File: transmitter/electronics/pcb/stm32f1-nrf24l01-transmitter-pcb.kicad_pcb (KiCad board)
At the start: 2 copper layers, 128 x 47 mm, 79 parts, among them J1 PA1/A1, J10 PB3, J11 PB4, J12 PB5, J13 PB6, J14 PB7, J15 PB8, J16 PB10, J17 PB11, J18 External charger LED, J19 BATTERY, J2 PA2/A2, J20 Red, J21 Blue, J22 POWER SWITCH, J23 USB, J24 UART, J25 SWD, J26 Buzzer, J27 NRF24 connector, J29 Meter, J3 PA3/A3, J30 LED, J4 PA4/A4, J5 PA5/A5, J6 PA6/A6, J7 PA7/A7, J8 PB0/A8, J9 PB1/A9, Q1 PMV30UN, SW1 RESET, U1 MCP1703A-3302, U2 LIPO_CHARGER_+_PROTECTION, U3 STM32F103CBT6, U4 MCP1703A-3302, Y1 8MHz

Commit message: Tweak layout
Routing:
- net /+USB: track 25.9 -> 37.4 mm
- net +3V3: track 294.7 -> 302.2 mm
- net /PB4: track 26.1 -> 24.3 mm
- net /PB3: track 31.9 -> 30.3 mm
- net /PB7: track 16.1 -> 14.6 mm
- net Net-(J18-Pad2): track 7.47 -> 6.13 mm
- net Net-(J22-Pad1): track 25.0 -> 24.1 mm
- net Net-(J18-Pad1): track 6.11 -> 5.37 mm

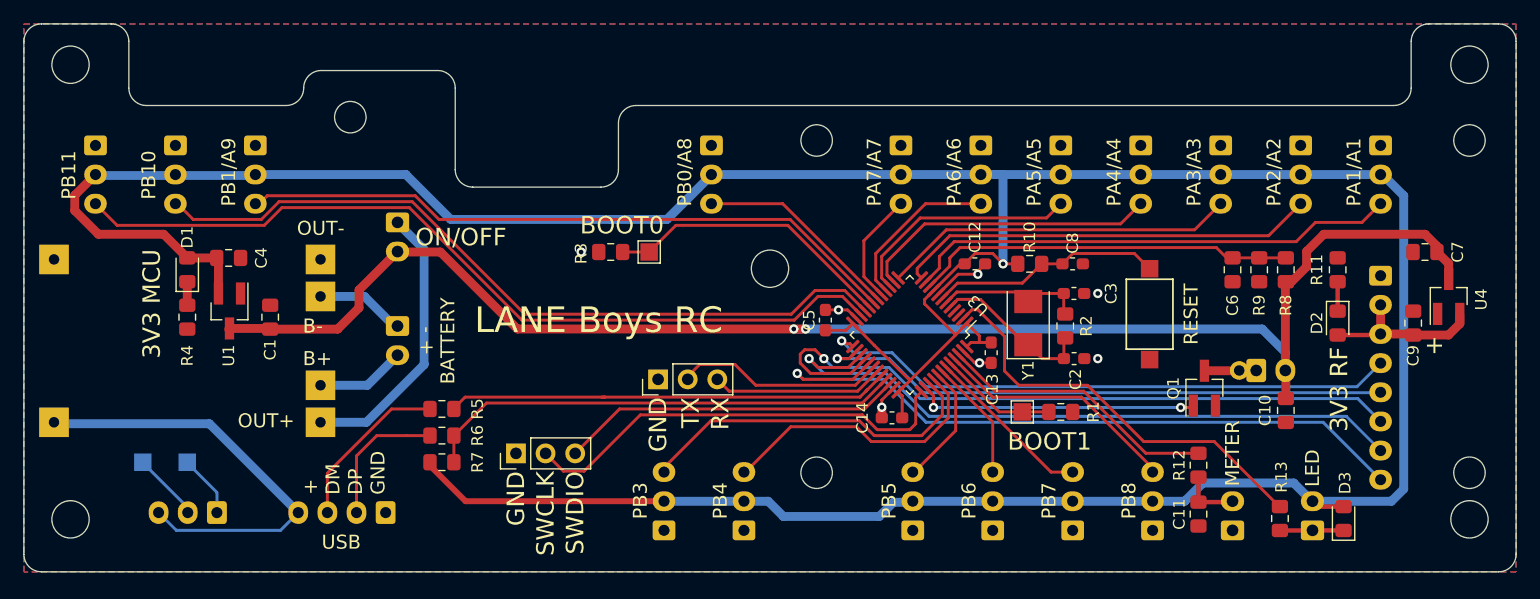
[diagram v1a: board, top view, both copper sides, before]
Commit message: Improve placement and silkscreen
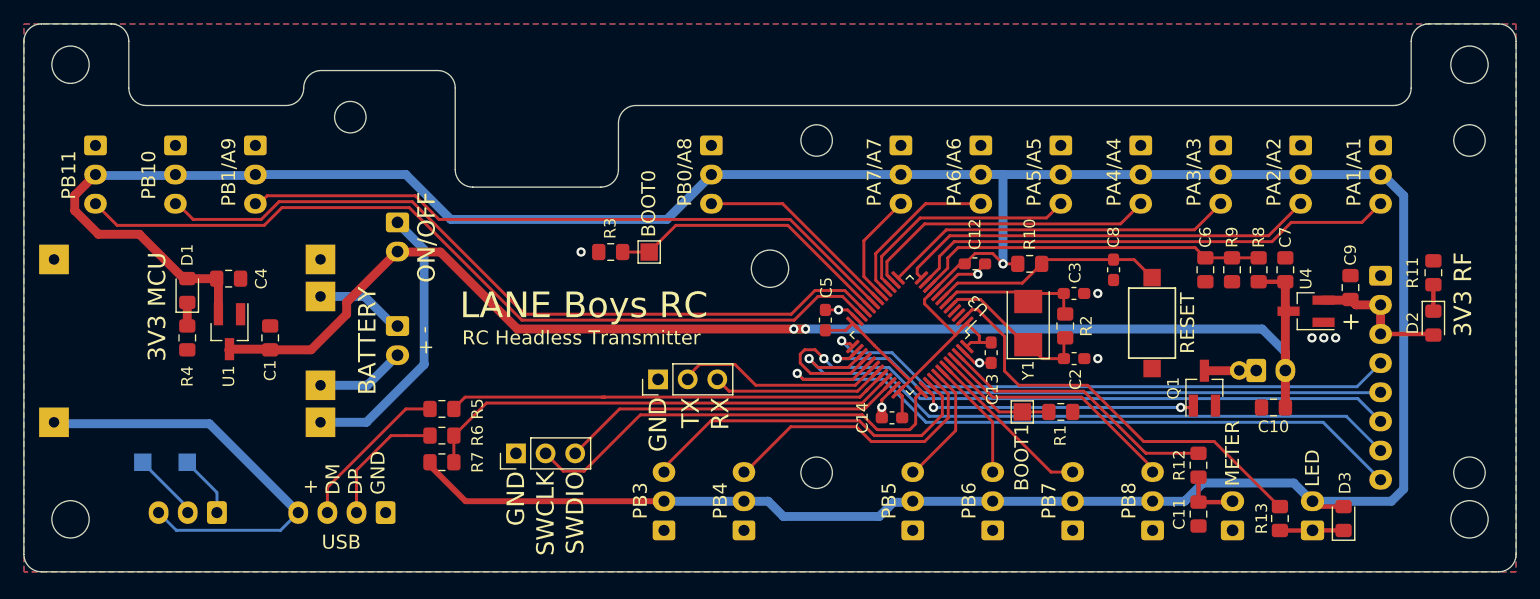
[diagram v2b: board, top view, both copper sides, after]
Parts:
- moved U4 12.3 mm to (181.0, 77.6), turned to 180 degrees
- moved C7 12.1 mm to (179.2, 74.1), turned to 90 degrees
- moved R11 8.21 mm to (191.9, 74.3)
- moved D2 8.21 mm to (191.9, 78.7)
- moved C9 6.18 mm to (184.8, 75.6)
- moved C8 3.55 mm to (164.5, 74.1), turned to 270 degrees
- moved C6 2.33 mm to (172.3, 74.1)
- moved R8 2.33 mm to (176.9, 74.1)
- moved R9 2.33 mm to (174.6, 74.1)
- moved C4 1.78 mm to (88.6, 74.9)
- moved D1 1.78 mm to (85.0, 75.9)
- moved U1 1.78 mm to (88.6, 79.4)
- moved C1 1.78 mm to (92.1, 79.9)
- moved R4 1.78 mm to (85.0, 79.9)
- moved C10 1.09 mm to (178.2, 85.9), turned to 180 degrees
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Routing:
- net VDD: track 129.6 -> 114.3 mm
- net /ADC0: track 32.7 -> 30.5 mm
- net /3V3_RF: track 14.3 -> 12.2 mm
- net +3V3: track 302.2 -> 302.9 mm
- net Net-(J23-Pad2): track 12.1 -> 11.4 mm
- net Net-(J23-Pad3): track 14.5 -> 13.7 mm
- net /NRST: track 19.9 -> 20.5 mm
- net GND: vias 7 -> 10
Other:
- board text added: "Blue"
- board text added: "RC Headless Transmitter"
- board text added: "Red"
- board text removed: "B+"
- board text removed: "B-"
- board text removed: "OUT+"
- board text removed: "OUT-"

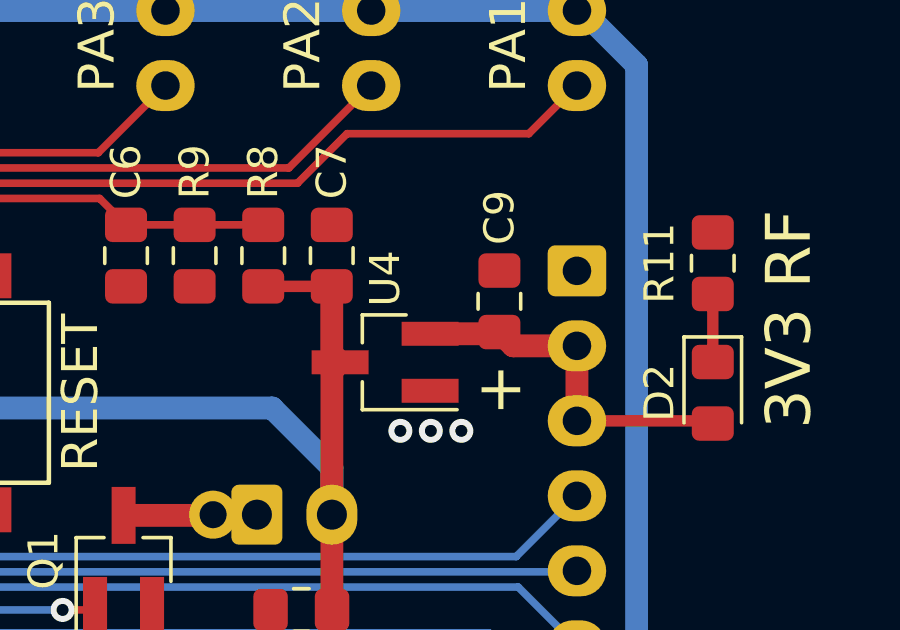
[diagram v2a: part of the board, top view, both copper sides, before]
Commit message: Fix DRC issue and add keepout area
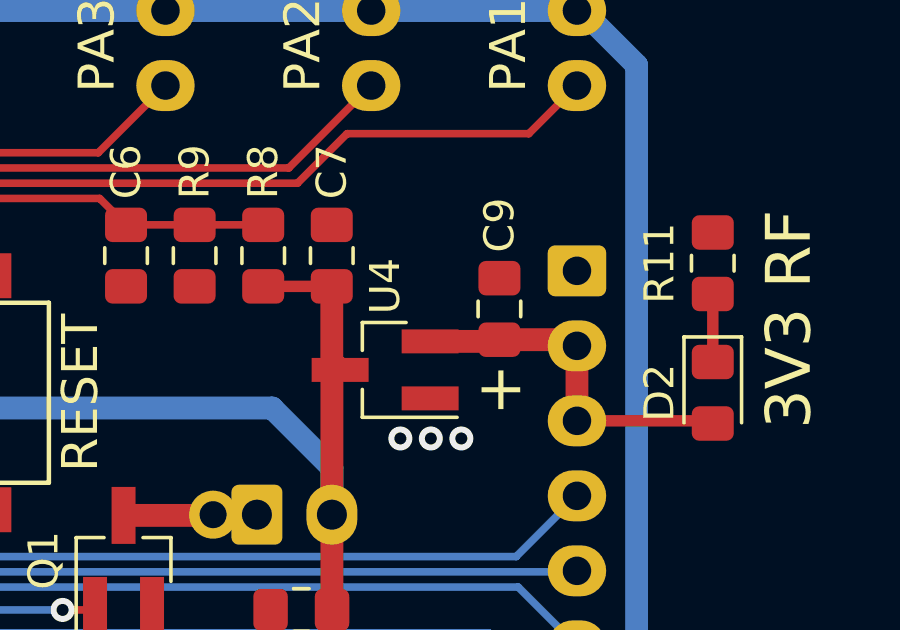
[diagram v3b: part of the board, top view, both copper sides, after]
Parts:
- moved C9 0.25 mm to (184.8, 75.9)
- moved U4 0.25 mm to (181.0, 77.9)
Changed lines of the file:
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@@
     (thickness 1.6)
     (drawings 99)
-    (tracks 405)
+    (tracks 404)
     (zones 0)
     (modules 79)
@@
     (47 F.CrtYd user)
     (48 B.Fab user)
-    (49 F.Fab user hide)
+    (49 F.Fab user)
   )
   (setup
@@
   )
   (module Package_TO_SOT_SMD:SOT-23_Handsoldering (layer F.Cu)
-    (at 180.982 77.648 180)
+    (at 180.982 77.902 180)
     (descr "SOT-23, Handsoldering")
     (tags SOT-23)
@@
   )
   (module Capacitor_SMD:C_0805_2012Metric_Pad1.15x1.40mm_HandSolder (layer F.Cu)
-    (at 184.792 75.616 90)
+    (at 184.792 75.87 90)
     (descr "Capacitor SMD 0805 (2012 Metric), square (rectangular) end terminal, IPC_7351 nominal with elongated pad for handsoldering. (Body size source: https://docs.google.com/spreadsheets/d/1BsfQQcO9C6DZCsRaXUlFlo91Tg2WpOkGARC1WS5S8t0/edit?usp=sharing), generated with kicad-footprint-generator")
     (tags "capacitor handsolder")
@@
   (via (at 144.591 85.889) (size 0.8) (drill 0.4) (layers F.Cu B.Cu) (net 1))
   (via (at 118.796 72.568) (size 0.8) (drill 0.4) (layers F.Cu B.Cu) (net 1))
-  (via (at 182.506 79.934) (size 0.8) (drill 0.4) (layers F.Cu B.Cu) (net 1))
-  (via (at 183.522 79.934) (size 0.8) (drill 0.4) (layers F.Cu B.Cu) (net 1))
-  (via (at 181.49 79.934) (size 0.8) (drill 0.4) (layers F.Cu B.Cu) (net 1))
+  (via (at 182.506 80.188) (size 0.8) (drill 0.4) (layers F.Cu B.Cu) (net 1))
+  (via (at 183.522 80.188) (size 0.8) (drill 0.4) (layers F.Cu B.Cu) (net 1))
+  (via (at 181.49 80.188) (size 0.8) (drill 0.4) (layers F.Cu B.Cu) (net 1))
   (segment (start 179.208 81.164) (end 179.208 82.728) (width 0.762) (layer B.Cu) (net 2))
   (segment (start 177.216 79.172) (end 179.208 81.164) (width 0.762) (layer B.Cu) (net 2))
@@
   (via (at 137.04 79.172) (size 0.8) (drill 0.4) (layers F.Cu B.Cu) (net 2))
   (segment (start 137.04 79.172) (end 138.056 79.172) (width 0.762) (layer B.Cu) (net 2))
-  (segment (start 179.208 77.922) (end 179.482 77.648) (width 0.762) (layer F.Cu) (net 2))
   (segment (start 179.208 82.728) (end 179.208 77.922) (width 0.762) (layer F.Cu) (net 2))
   (segment (start 179.208 85.898) (end 179.213 85.903) (width 0.762) (layer F.Cu) (net 2))
   (segment (start 179.208 82.728) (end 179.208 85.898) (width 0.762) (layer F.Cu) (net 2))
   (segment (start 176.927 75.126) (end 176.918 75.117) (width 0.762) (layer F.Cu) (net 2))
-  (segment (start 179.204 77.37) (end 179.204 75.117) (width 0.762) (layer F.Cu) (net 2))
-  (segment (start 179.482 77.648) (end 179.204 77.37) (width 0.762) (layer F.Cu) (net 2))
   (segment (start 176.918 75.117) (end 179.204 75.117) (width 0.381) (layer F.Cu) (net 2))
   (segment (start 88.561 80.977) (end 88.636 80.902) (width 0.762) (layer F.Cu) (net 2) (status 30))
@@
   (segment (start 103.044 72.528) (end 103.048 72.528) (width 0.762) (layer F.Cu) (net 2))
   (segment (start 95.629 80.959) (end 98.686 77.902) (width 0.762) (layer F.Cu) (net 2))
+  (segment (start 179.204 77.624) (end 179.482 77.902) (width 0.762) (layer F.Cu) (net 2))
+  (segment (start 179.204 75.117) (end 179.204 77.624) (width 0.762) (layer F.Cu) (net 2))
   (segment (start 160.212 80.047) (end 160.325 79.934) (width 0.254) (layer F.Cu) (net 3) (status 30))
   (segment (start 160.212 81.712) (end 160.212 80.047) (width 0.254) (layer F.Cu) (net 3) (status 30))
@@
   (segment (start 156.344 83.998) (end 162.23 83.998) (width 0.254) (layer F.Cu) (net 53))
   (segment (start 187.376 77.1) (end 187.376 79.6) (width 0.762) (layer F.Cu) (net 56) (status 30))
-  (segment (start 184.735 76.698) (end 184.792 76.641) (width 0.762) (layer F.Cu) (net 56))
-  (segment (start 182.482 76.698) (end 184.735 76.698) (width 0.762) (layer F.Cu) (net 56))
-  (segment (start 185.251 77.1) (end 187.376 77.1) (width 0.762) (layer F.Cu) (net 56))
-  (segment (start 184.792 76.641) (end 185.251 77.1) (width 0.762) (layer F.Cu) (net 56))
   (segment (start 191.815 79.6) (end 191.904 79.689) (width 0.381) (layer F.Cu) (net 56))
   (segment (start 187.376 79.6) (end 191.815 79.6) (width 0.381) (layer F.Cu) (net 56))
+  (segment (start 184.735 76.952) (end 184.792 76.895) (width 0.762) (layer F.Cu) (net 56))
+  (segment (start 182.482 76.952) (end 184.735 76.952) (width 0.762) (layer F.Cu) (net 56))
+  (segment (start 187.171 76.895) (end 187.376 77.1) (width 0.762) (layer F.Cu) (net 56))
+  (segment (start 184.792 76.895) (end 187.171 76.895) (width 0.762) (layer F.Cu) (net 56))
   (zone (net 1) (net_name GND) (layer F.Cu) (hatch edge 0.508)
     (connect_pads (clearance 0.508))
@@
       )
     )
+  )
+  (zone (net 0) (net_name "") (layers F&B.Cu) (hatch edge 0.508)
+    (connect_pads (clearance 0.508))
+    (min_thickness 0.254)
+    (keepout (tracks allowed) (vias not_allowed) (copperpour allowed))
+    (fill (arc_segments 32) (thermal_gap 0.508) (thermal_bridge_width 0.508))
+    (polygon
+      (pts
+        (xy 115.958 78.41) (xy 113.926 78.41) (xy 113.926 66.98) (xy 115.958 66.98)
+      )
+    )

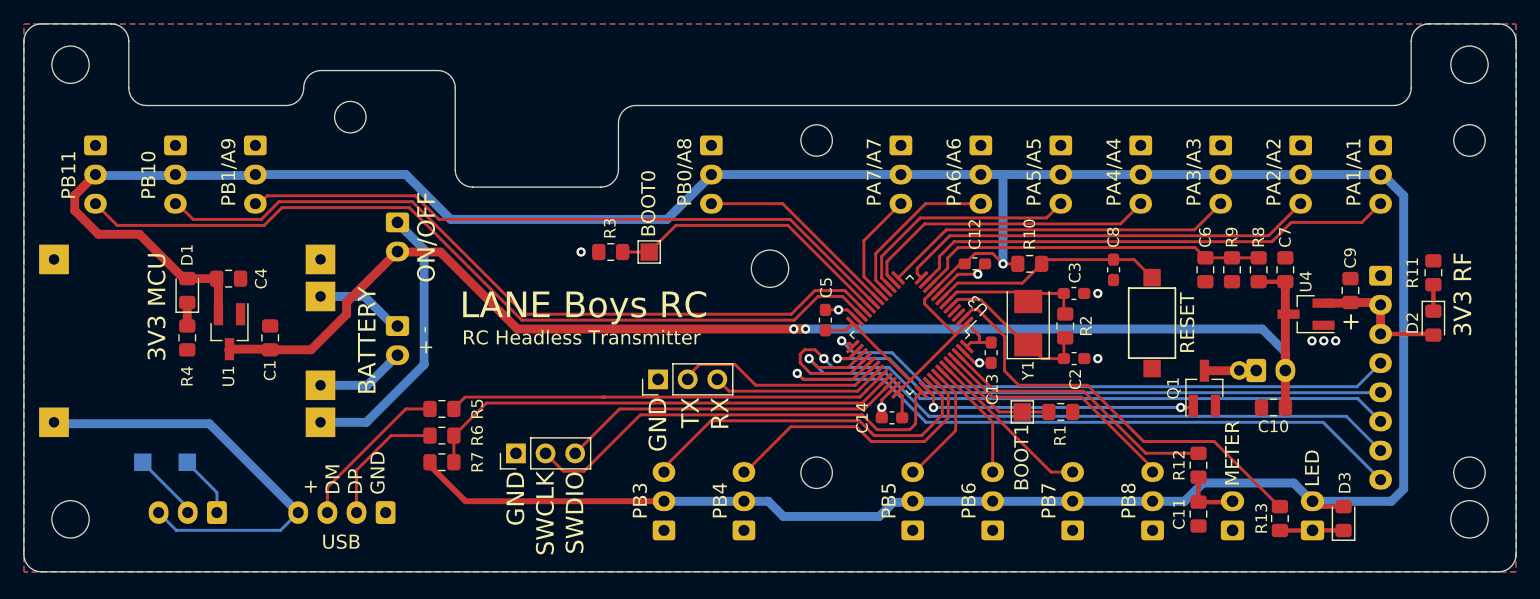
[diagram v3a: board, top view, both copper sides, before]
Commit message: Improve layout and silkscreen further
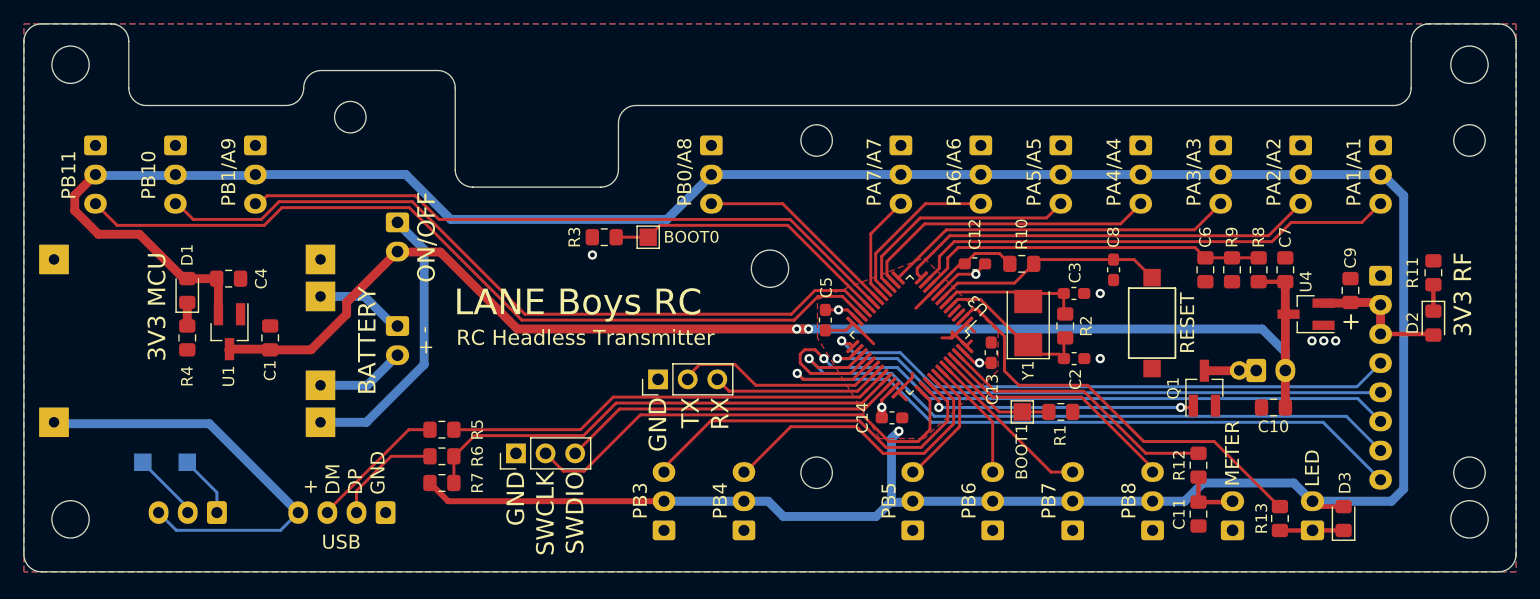
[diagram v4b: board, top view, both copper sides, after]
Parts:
- moved R5 1.78 mm to (106.9, 87.8)
- moved R6 1.78 mm to (106.9, 90.1)
- moved R7 1.78 mm to (106.9, 92.4)
- moved R3 1.38 mm to (120.8, 71.3)
- moved TP2 1.27 mm to (124.5, 71.3), turned to 270 degrees
- moved R10 0.68 mm to (156.6, 73.6)
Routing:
- net +3V3: track 302.9 -> 284.4 mm
- net /SWDCLK: track 38.1 -> 40.5 mm
- net Net-(J23-Pad2): track 11.4 -> 9.39 mm
- net /PB4: track 24.3 -> 26.1 mm
- net /PB3: track 30.3 -> 32.1 mm
- net Net-(J23-Pad3): track 13.7 -> 12.1 mm
- net /USBDP: track 41.3 -> 42.1 mm
- added copper zone on F.Cu, net +3V3
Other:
- board text removed: "BAT"

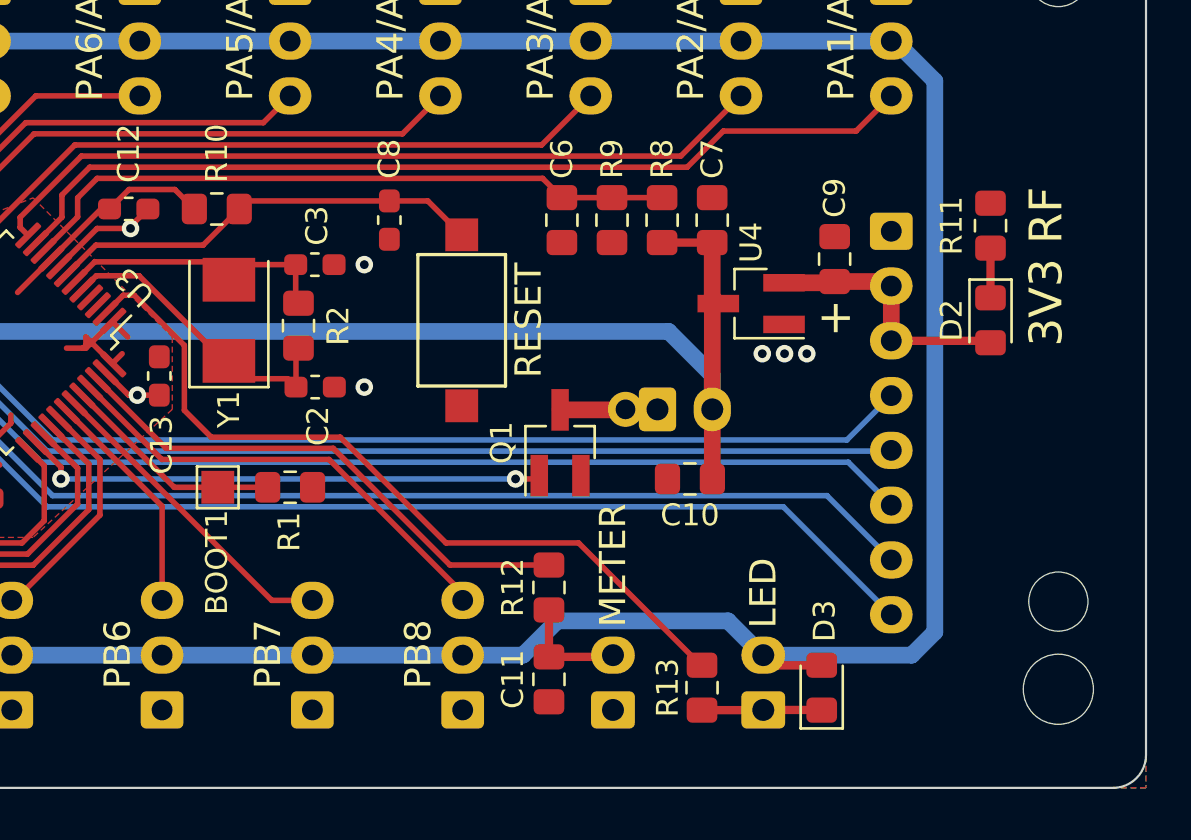
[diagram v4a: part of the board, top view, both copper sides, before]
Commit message: Move components out of connector courtyard
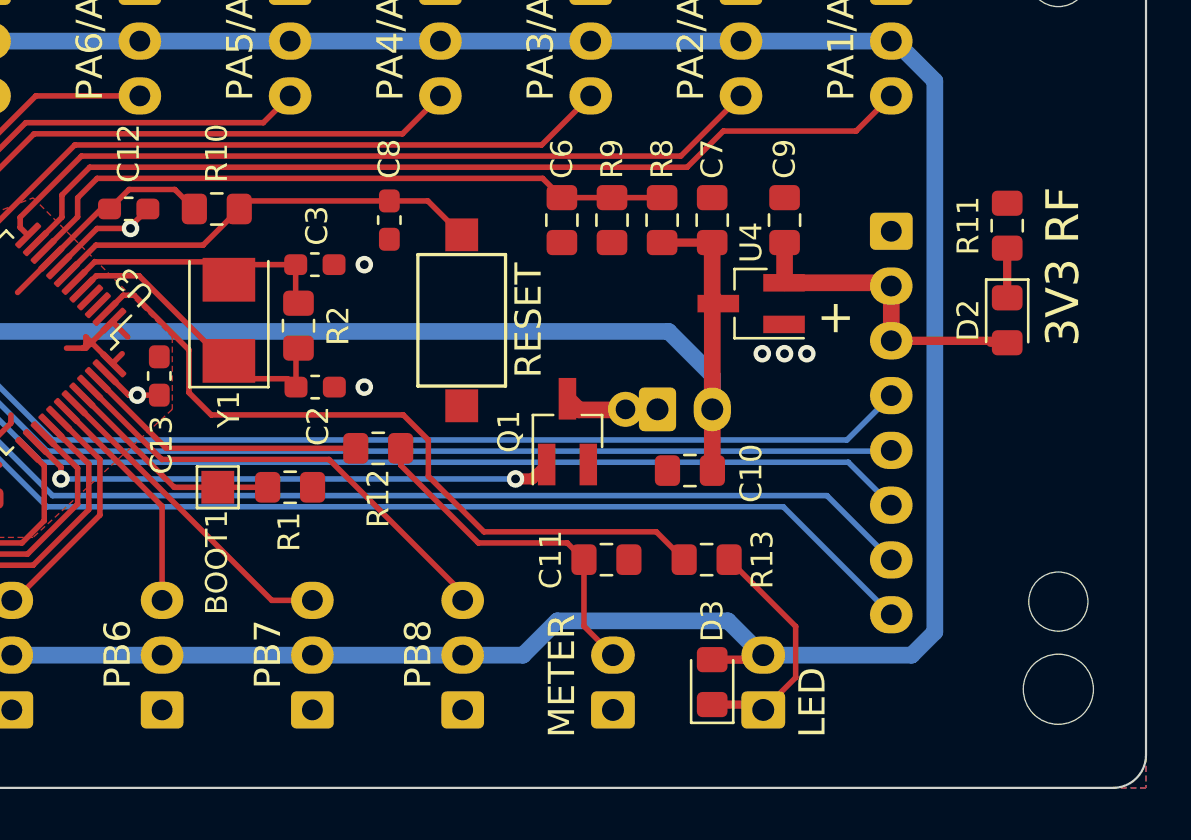
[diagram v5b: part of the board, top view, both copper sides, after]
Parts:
- moved R12 10.1 mm to (164.0, 84.5), turned to 0 degrees
- moved C11 6.06 mm to (174.4, 89.6), turned to 0 degrees
- moved R13 5.85 mm to (178.9, 89.6), turned to 180 degrees
- moved D3 5.00 mm to (179.2, 95.2)
- moved C9 2.90 mm to (182.5, 74.1)
- moved D2 0.76 mm to (192.7, 78.7)
- moved R11 0.76 mm to (192.7, 74.3)
- moved Q1 0.61 mm to (172.6, 83.7)
- moved C10 0.38 mm to (178.2, 85.5)
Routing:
- net Net-(C11-Pad1): track 5.09 -> 15.9 mm
- net /METER: track 24.1 -> 13.3 mm
- net Net-(D3-Pad1): track 5.47 -> 11.5 mm
- net /3V3_RF: track 12.1 -> 15.4 mm
- net /LED: track 36.3 -> 33.8 mm
- net Net-(J26-Pad1): track 4.45 -> 5.79 mm
- net /BUZZER: track 24.1 -> 24.8 mm
- net +3V3: track 284.4 -> 284.9 mm
